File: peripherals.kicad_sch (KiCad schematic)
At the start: 23 parts, among them J10 0533980471, J12 QTH-030-01-L-D-A, J9 QSH-030-01-L-D-A, U10 NTS0102, U2 MAX3051, U33 NTS0102, U9 NTS0102

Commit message: Layout cleanup, silk
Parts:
- TP29, TP30, TP31, TP32, TP33: footprint JetsonCarrier:TP_SMD_0.75mm -> TestPoint:TestPoint_Pad_D1.0mm
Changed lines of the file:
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@@
 			)
 		)
-		(property "Footprint" "JetsonCarrier:TP_SMD_0.75mm"
+		(property "Footprint" "TestPoint:TestPoint_Pad_D1.0mm"
 			(at 167.64 255.905 0)
 			(hide yes)
@@
 			)
 		)
-		(property "Footprint" "JetsonCarrier:TP_SMD_0.75mm"
+		(property "Footprint" "TestPoint:TestPoint_Pad_D1.0mm"
 			(at 260.35 245.745 0)
 			(hide yes)
@@
 			)
 		)
-		(property "Footprint" "JetsonCarrier:TP_SMD_0.75mm"
+		(property "Footprint" "TestPoint:TestPoint_Pad_D1.0mm"
 			(at 260.35 240.665 0)
 			(hide yes)
@@
 			)
 		)
-		(property "Footprint" "JetsonCarrier:TP_SMD_0.75mm"
+		(property "Footprint" "TestPoint:TestPoint_Pad_D1.0mm"
 			(at 167.64 253.365 0)
 			(hide yes)
@@
 			)
 		)
-		(property "Footprint" "JetsonCarrier:TP_SMD_0.75mm"
+		(property "Footprint" "TestPoint:TestPoint_Pad_D1.0mm"
 			(at 167.64 258.445 0)
 			(hide yes)

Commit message: route all diff pairs, length tuning
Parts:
- removed TP29, TP31: TP_0.75mm_SMD, TestPoint:TestPoint_Pad_D1.0mm, symbol Connector:TestPoint
- removed U10, U33, U9: NTS0102, Argus-IC:NXP_XSON-8, symbol JetsonCarrier:NTS0102
- added U23, U24, U25: NTS0102, Argus-IC:NXP_XSON-8, symbol Argus-IC:NTS0102
- renumbered C44 to C63, C40 to C64, C53 to C65, C48 to C66, C41 to C67, C54 to C68, C55 to C69, H9 to H6, H10 to H7, J10 to J12, J9 to J13, J12 to J14, R108 to R102, R20 to R103, TP30 to TP18, TP32 to TP19, TP33 to TP20, U2 to U26
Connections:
- net +1V8: now also U23.3 (VCC_{A}), U23.6 (OE), U24.3 (VCC_{A}), U24.6 (OE), U25.3 (VCC_{A}), U25.6 (OE)
- net +3V3: now also U24.7 (VCC_{B}), U25.7 (VCC_{B})
- net +5V: now also U23.7 (VCC_{B})
- net FAN_PWM: now also U23.4 (A_{2})
- net FAN_PWM_5V: now also U23.1 (B_{2})
- net FAN_TACH: now also U23.5 (A_{1})
- net FAN_TACH_5V: now also U23.8 (B_{1})
- net GND: now also U23.2 (GND), U24.2 (GND), U25.2 (GND)
- net MB_JETSON_CS: now also U25.8 (B_{1})
- net MB_SPI_MISO: now also U25.1 (B_{2})
- net MB_SPI_MOSI: now also U24.8 (B_{1})
- net MB_SPI_SCK: now also U24.1 (B_{2})
- net SPI0_MISO: now also U25.4 (A_{2})
- net SPI0_MOSI: now also U24.5 (A_{1})
- net SPI0_SCK: now also U24.4 (A_{2})
- net ~{SPI0_CS}: now also U25.5 (A_{1})

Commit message: DRC errors resolved, silk placement
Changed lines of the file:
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@@
-	(wire
-		(pts
-			(xy 304.8 142.24) (xy 328.93 142.24)
-		)
-		(stroke
-			(width 0)
-			(type default)
-		)
-	)
 	(wire
 		(pts

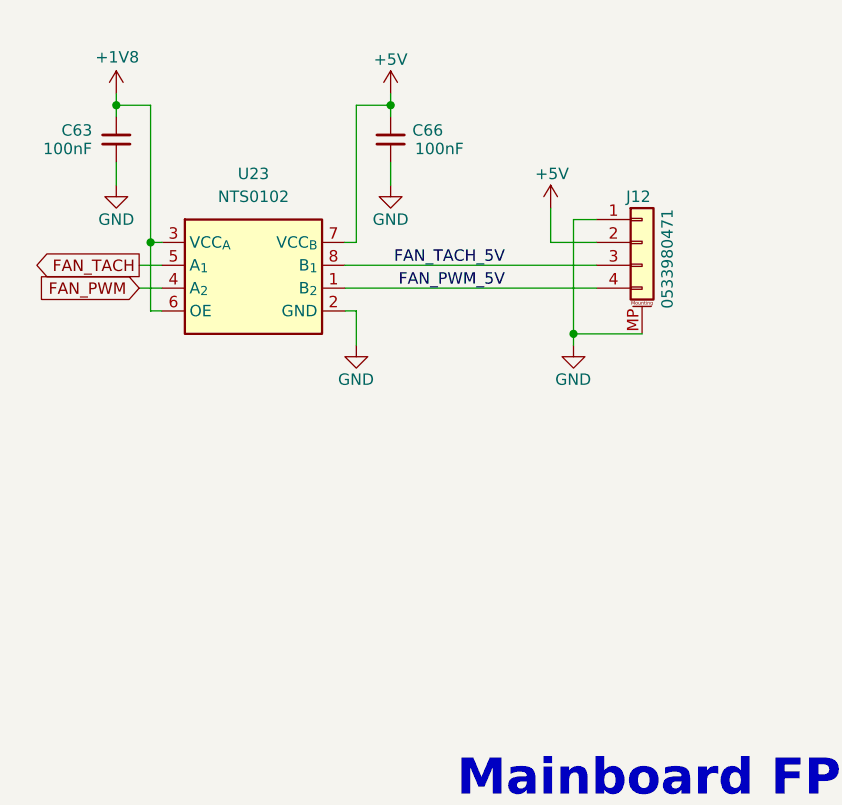
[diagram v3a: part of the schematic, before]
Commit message: Move parts under SoM to bottom for thinner module connector
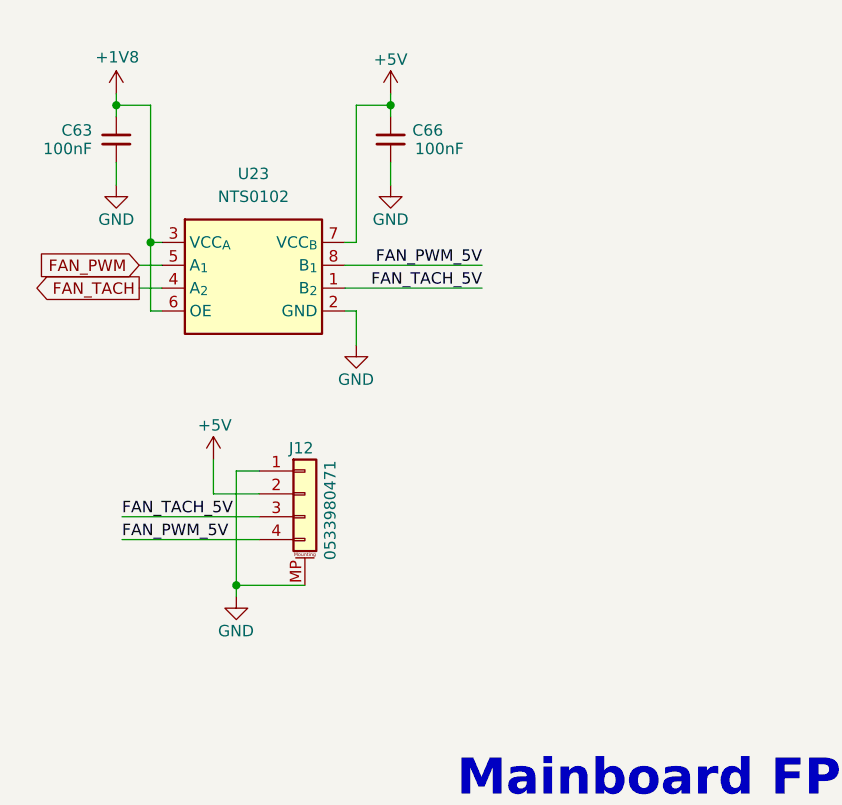
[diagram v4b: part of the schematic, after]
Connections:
- net FAN_PWM: now also U23.5 (A_{1}); no longer U23.4 (A_{2})
- net FAN_PWM_5V: now also U23.8 (B_{1}); no longer U23.1 (B_{2})
- net FAN_TACH: now also U23.4 (A_{2}); no longer U23.5 (A_{1})
- net FAN_TACH_5V: now also U23.1 (B_{2}); no longer U23.8 (B_{1})
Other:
- moved on the sheet: J12
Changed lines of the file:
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@@
 	)
 	(junction
-		(at 92.71 144.145)
+		(at 55.245 172.085)
 		(diameter 0)
 		(color 0 0 0 0)
@@
 	(wire
 		(pts
+			(xy 57.785 164.465) (xy 42.545 164.465)
+		)
+		(stroke
+			(width 0)
+			(type default)
+		)
+	)
+	(wire
+		(pts
 			(xy 304.8 132.08) (xy 322.58 132.08)
 		)
@@
 	(wire
 		(pts
-			(xy 92.71 131.445) (xy 95.25 131.445)
+			(xy 55.245 159.385) (xy 57.785 159.385)
 		)
 		(stroke
@@
 	(wire
 		(pts
+			(xy 67.31 139.065) (xy 82.55 139.065)
+		)
+		(stroke
+			(width 0)
+			(type default)
+		)
+	)
+	(wire
+		(pts
 			(xy 165.735 91.44) (xy 184.785 91.44)
 		)
@@
 	(wire
 		(pts
+			(xy 57.785 167.005) (xy 42.545 167.005)
+		)
+		(stroke
+			(width 0)
+			(type default)
+		)
+	)
+	(wire
+		(pts
 			(xy 322.58 91.44) (xy 304.8 91.44)
 		)
@@
 	(wire
 		(pts
-			(xy 67.31 136.525) (xy 95.25 136.525)
-		)
-		(stroke
-			(width 0)
-			(type default)
-		)
-	)
-	(wire
-		(pts
 			(xy 165.735 109.22) (xy 184.785 109.22)
 		)
@@
 	(wire
 		(pts
-			(xy 92.71 144.145) (xy 92.71 145.415)
+			(xy 55.245 172.085) (xy 55.245 173.355)
 		)
 		(stroke
@@
 	(wire
 		(pts
-			(xy 92.71 144.145) (xy 100.33 144.145)
+			(xy 55.245 172.085) (xy 62.865 172.085)
 		)
 		(stroke
@@
 	(wire
 		(pts
-			(xy 67.31 139.065) (xy 95.25 139.065)
-		)
-		(stroke
-			(width 0)
-			(type default)
-		)
-	)
-	(wire
-		(pts
 			(xy 273.05 83.82) (xy 292.1 83.82)
 		)
@@
 	(wire
 		(pts
-			(xy 90.17 130.175) (xy 90.17 133.985)
+			(xy 52.705 158.115) (xy 52.705 161.925)
 		)
 		(stroke
@@
 	(wire
 		(pts
-			(xy 90.17 133.985) (xy 95.25 133.985)
+			(xy 52.705 161.925) (xy 57.785 161.925)
 		)
 		(stroke
@@
 	(wire
 		(pts
-			(xy 92.71 131.445) (xy 92.71 144.145)
+			(xy 55.245 159.385) (xy 55.245 172.085)
 		)
 		(stroke
@@
 	(wire
 		(pts
+			(xy 67.31 136.525) (xy 82.55 136.525)
+		)
+		(stroke
+			(width 0)
+			(type default)
+		)
+	)
+	(wire
+		(pts
 			(xy 165.735 101.6) (xy 184.785 101.6)
 		)
@@
 	)
 	(label "FAN_TACH_5V"
-		(at 85.09 136.525 180)
+		(at 82.55 139.065 180)
 		(effects
 			(font
@@
 	)
 	(label "FAN_PWM_5V"
-		(at 85.09 139.065 180)
+		(at 82.55 136.525 180)
 		(effects
 			(font
@@
 		)
 	)
+	(label "FAN_PWM_5V"
+		(at 42.545 167.005 0)
+		(effects
+			(font
+				(size 1.27 1.27)
+			)
+			(justify left bottom)
+		)
+	)
 	(label "Pin_54"
 		(at 197.485 144.78 0)
@@
 		)
 	)
+	(label "FAN_TACH_5V"
+		(at 42.545 164.465 0)
+		(effects
+			(font
+				(size 1.27 1.27)
+			)
+			(justify left bottom)
+		)
+	)
 	(label "Pin_43"
 		(at 184.785 132.08 180)
@@
 	(global_label "FAN_TACH"
 		(shape output)
-		(at 44.45 136.525 180)
+		(at 44.45 139.065 180)
 		(fields_autoplaced yes)
 		(effects
@@
 		)
 		(property "Intersheetrefs" "${INTERSHEET_REFS}"
-			(at 32.905 136.6044 0)
+			(at 32.905 138.9856 0)
 			(show_name no)
 			(do_not_autoplace no)
@@
 	(global_label "FAN_PWM"
 		(shape input)
-		(at 44.45 139.065 180)
+		(at 44.45 136.525 180)
 		(fields_autoplaced yes)
 		(effects
@@
 		)
 		(property "Intersheetrefs" "${INTERSHEET_REFS}"
-			(at 33.3888 139.1444 0)
+			(at 33.3888 136.4456 0)
 			(show_name no)
 			(do_not_autoplace no)
@@
 	(symbol
 		(lib_id "power:+5V")
-		(at 90.17 130.175 0)
+		(at 52.705 158.115 0)
 		(unit 1)
 		(body_style 1)
@@
 		(dnp no)
 		(property "Reference" "#PWR0168"
-			(at 90.17 133.985 0)
+			(at 52.705 161.925 0)
 			(hide yes)
 			(show_name no)
@@
 		)
 		(property "Value" "+5V"
-			(at 92.202 126.365 0)
+			(at 54.737 154.305 0)
 			(show_name no)
 			(do_not_autoplace no)
@@
 		)
 		(property "Footprint" ""
-			(at 90.17 130.175 0)
+			(at 52.705 158.115 0)
 			(hide yes)
 			(show_name no)
@@
 		)
 		(property "Datasheet" ""
-			(at 90.17 130.175 0)
+			(at 52.705 158.115 0)
 			(hide yes)
 			(show_name no)
@@
 		)
 		(property "Description" "Power symbol creates a global label with name \"+5V\""
-			(at 90.17 130.175 0)
+			(at 52.705 158.115 0)
 			(hide yes)
 			(show_name no)
@@
 	(symbol
 		(lib_id "Connector_Generic_MountingPin:Conn_01x04_MountingPin")
-		(at 100.33 133.985 0)
+		(at 62.865 161.925 0)
 		(unit 1)
 		(body_style 1)
@@
 		(dnp no)
 		(property "Reference" "J12"
-			(at 98.552 128.905 0)
+			(at 61.087 156.845 0)
 			(show_name no)
 			(do_not_autoplace no)
@@
 		)
 		(property "Value" "0533980471"
-			(at 103.886 141.351 90)
+			(at 66.421 169.291 90)
 			(show_name no)
 			(do_not_autoplace no)
@@
 		)
 		(property "Footprint" "Connector_Molex:Molex_PicoBlade_53398-0471_1x04-1MP_P1.25mm_Vertical"
-			(at 100.33 133.985 0)
+			(at 62.865 161.925 0)
 			(hide yes)
 			(show_name no)
@@
 		)
 		(property "Datasheet" ""
-			(at 100.33 133.985 0)
+			(at 62.865 161.925 0)
 			(hide yes)
 			(show_name no)
@@
 		)
 		(property "Description" "Generic connectable mounting pin connector, single row, 01x04, script generated (kicad-library-utils/schlib/autogen/connector/)"
-			(at 100.33 133.985 0)
+			(at 62.865 161.925 0)
 			(hide yes)
 			(show_name no)
@@
 		)
 		(property "MPN" "C225106"
-			(at 103.378 141.097 90)
+			(at 65.913 169.037 90)
 			(hide yes)
 			(show_name no)
@@
 	(symbol
 		(lib_id "power:GND")
-		(at 92.71 145.415 0)
+		(at 55.245 173.355 0)
 		(unit 1)
 		(body_style 1)
@@
 		(dnp no)
 		(property "Reference" "#PWR0169"
-			(at 92.71 151.765 0)
+			(at 55.245 179.705 0)
 			(hide yes)
 			(show_name no)
@@
 		)
 		(property "Value" "GND"
-			(at 90.678 149.225 0)
+			(at 53.213 177.165 0)
 			(show_name no)
 			(do_not_autoplace no)
@@
 		)
 		(property "Footprint" ""
-			(at 92.71 145.415 0)
+			(at 55.245 173.355 0)
 			(hide yes)
 			(show_name no)
@@
 		)
 		(property "Datasheet" ""
-			(at 92.71 145.415 0)
+			(at 55.245 173.355 0)
 			(hide yes)
 			(show_name no)
@@
 		)
 		(property "Description" "Power symbol creates a global label with name \"GND\" , ground"
-			(at 92.71 145.415 0)
+			(at 55.245 173.355 0)
 			(hide yes)
 			(show_name no)
@@
 		)
 		(property "Author" "Antmicro"
-			(at 101.6 153.035 0)
+			(at 64.135 180.975 0)
 			(hide yes)
 			(show_name no)
@@
 		)
 		(property "License" "Apache-2.0"
-			(at 101.6 155.575 0)
+			(at 64.135 183.515 0)
 			(hide yes)
 			(show_name no)

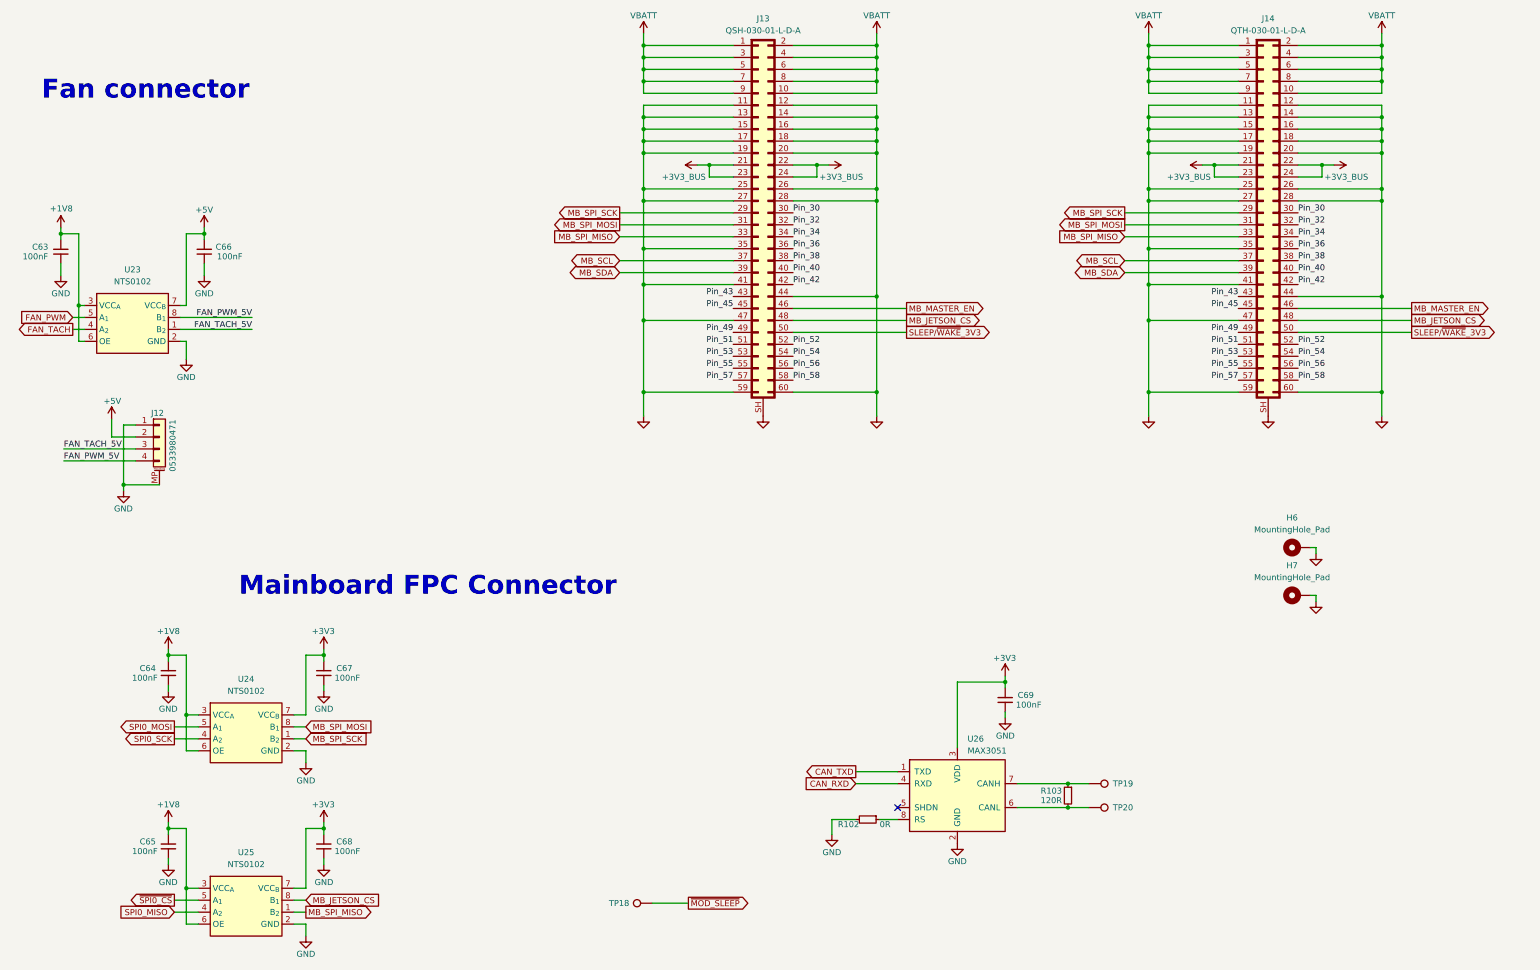
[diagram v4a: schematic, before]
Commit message: Replace current monitor w/ INA226 (addr = 0x42)
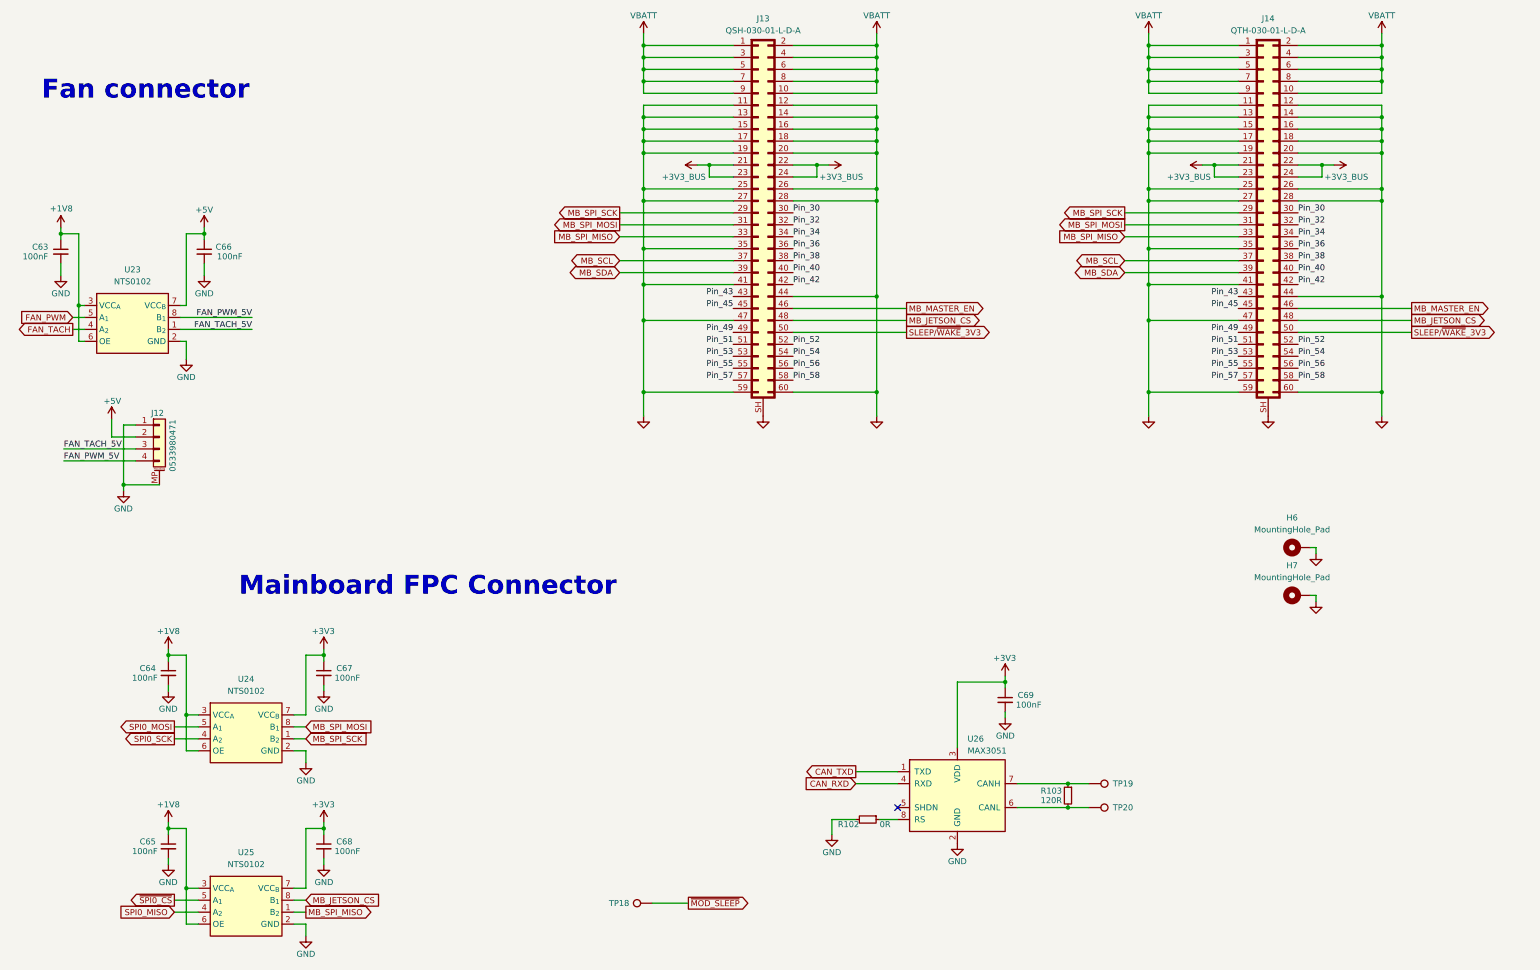
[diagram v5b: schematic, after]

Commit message: Final BOM changes, gerbers
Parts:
- C63, C64, C65, C66, C67, C68, C69: LCSC (none) -> C14663
- J12: LCSC (none) -> C17617036
- J13: LCSC (none) -> C2909821
- J14: LCSC (none) -> C2843756
- R102: LCSC (none) -> C21189
- R103: LCSC (none) -> C22787
- U23, U24, U25: LCSC (none) -> C2687851
- U26: LCSC (none) -> C112005
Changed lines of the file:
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@@
 			)
 		)
+		(property "LCSC" "C22787"
+			(at 254.635 237.109 0)
+			(effects
+				(font
+					(size 1.27 1.27)
+				)
+				(hide yes)
+			)
+		)
 		(pin "2"
 		)
@@
 			)
 		)
+		(property "LCSC" "C2687851"
+			(at 57.15 126.365 0)
+			(effects
+				(font
+					(size 1.27 1.27)
+				)
+				(hide yes)
+			)
+		)
 		(pin "4"
 		)
@@
 			)
 		)
+		(property "LCSC" "C2687851"
+			(at 81.28 213.36 0)
+			(effects
+				(font
+					(size 1.27 1.27)
+				)
+				(hide yes)
+			)
+		)
 		(pin "4"
 		)
@@
 			)
 		)
+		(property "LCSC" "C21189"
+			(at 207.01 244.983 0)
+			(effects
+				(font
+					(size 1.27 1.27)
+				)
+				(hide yes)
+			)
+		)
 		(pin "1"
 		)
@@
 			)
 		)
+		(property "LCSC" "C2843756"
+			(at 298.45 73.025 0)
+			(effects
+				(font
+					(size 1.27 1.27)
+				)
+				(hide yes)
+			)
+		)
 		(pin "19"
 		)
@@
 			)
 		)
+		(property "LCSC" "C14663"
+			(at 103.886 211.074 0)
+			(effects
+				(font
+					(size 1.27 1.27)
+				)
+				(hide yes)
+			)
+		)
 		(pin "1"
 		)
@@
 			)
 		)
+		(property "LCSC" "C112005"
+			(at 234.5533 226.06 0)
+			(effects
+				(font
+					(size 1.27 1.27)
+				)
+				(hide yes)
+			)
+		)
 		(pin "2"
 		)
@@
 			)
 		)
+		(property "LCSC" "C14663"
+			(at 103.886 247.904 0)
+			(effects
+				(font
+					(size 1.27 1.27)
+				)
+				(hide yes)
+			)
+		)
 		(pin "1"
 		)
@@
 			)
 		)
+		(property "LCSC" "C14663"
+			(at 35.814 121.539 0)
+			(effects
+				(font
+					(size 1.27 1.27)
+				)
+				(hide yes)
+			)
+		)
 		(pin "1"
 		)
@@
 			)
 		)
+		(property "LCSC" "C14663"
+			(at 58.674 211.074 0)
+			(effects
+				(font
+					(size 1.27 1.27)
+				)
+				(hide yes)
+			)
+		)
 		(pin "1"
 		)
@@
 			)
 		)
+		(property "LCSC" "C14663"
+			(at 58.674 247.904 0)
+			(effects
+				(font
+					(size 1.27 1.27)
+				)
+				(hide yes)
+			)
+		)
 		(pin "1"
 		)
@@
 			)
 		)
+		(property "LCSC" "C14663"
+			(at 78.232 121.539 0)
+			(effects
+				(font
+					(size 1.27 1.27)
+				)
+				(hide yes)
+			)
+		)
 		(pin "1"
 		)
@@
 			)
 		)
+		(property "LCSC" "C14663"
+			(at 248.666 216.789 0)
+			(effects
+				(font
+					(size 1.27 1.27)
+				)
+				(hide yes)
+			)
+		)
 		(pin "1"
 		)
@@
 			)
 		)
+		(property "LCSC" "C17617036"
+			(at 61.087 156.845 0)
+			(effects
+				(font
+					(size 1.27 1.27)
+				)
+				(hide yes)
+			)
+		)
 		(pin "1"
 		)
@@
 			)
 		)
+		(property "LCSC" "C2687851"
+			(at 81.28 250.19 0)
+			(effects
+				(font
+					(size 1.27 1.27)
+				)
+				(hide yes)
+			)
+		)
 		(pin "4"
 		)
@@
 			)
 		)
+		(property "LCSC" "C2909821"
+			(at 191.135 73.025 0)
+			(effects
+				(font
+					(size 1.27 1.27)
+				)
+				(hide yes)
+			)
+		)
